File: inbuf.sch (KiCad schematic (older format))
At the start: 21 parts, among them J8 Conn_02x03_Odd_Even, U6 NE5532, U7 NE5532

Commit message: Board is placed and about half-routed
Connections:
- net OUT1: now also U7.1, U7.2 (-); no longer U6.6 (-), U6.7
- net OUT2: now also U7.6 (-), U7.7; no longer U7.1, U7.2 (-)
- net at C34.1, R33.1, R35.1: now also U6.5 (+); no longer U7.5 (+)
- net at R34.2, R36.2: now also U6.6 (-); no longer U7.6 (-)
- net at R32.1, R34.1: now also U6.7; no longer U7.7
- net at J8.4 (Pin_4), R30.1: now also U7.3 (+); no longer U6.5 (+)
- net at J8.3 (Pin_3), R31.1: now also U7.5 (+); no longer U7.3 (+)
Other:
- moved on the sheet: U6B, U7A, U7B
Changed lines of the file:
@@
 L Amplifier_Operational:NE5532 U7
 U 2 1 6159C1D0
-P 3700 4400
-F 0 "U7" H 3700 4800 50  0000 C CNN
-F 1 "NE5532" H 3750 4700 50  0000 C CNN
-F 2 "Housings_DIP:DIP-8_W7.62mm_Socket" H 3700 4400 50  0001 C CNN
-F 3 "http://www.ti.com/lit/ds/symlink/ne5532.pdf" H 3700 4400 50  0001 C CNN
-	2    3700 4400
+P 5950 4400
+F 0 "U7" H 5950 4800 50  0000 C CNN
+F 1 "NE5532" H 6000 4700 50  0000 C CNN
+F 2 "Housings_DIP:DIP-8_W7.62mm_Socket" H 5950 4400 50  0001 C CNN
+F 3 "http://www.ti.com/lit/ds/symlink/ne5532.pdf" H 5950 4400 50  0001 C CNN
+	2    5950 4400
 	1    0    0    -1
 $EndComp
@@
 L Amplifier_Operational:NE5532 U7
 U 1 1 6190D92F
-P 5950 4400
-F 0 "U7" H 5900 4800 50  0000 C CNN
-F 1 "NE5532" H 5950 4700 50  0000 C CNN
-F 2 "Housings_DIP:DIP-8_W7.62mm_Socket" H 5950 4400 50  0001 C CNN
-F 3 "http://www.ti.com/lit/ds/symlink/ne5532.pdf" H 5950 4400 50  0001 C CNN
-	1    5950 4400
+P 5950 1800
+F 0 "U7" H 5900 2200 50  0000 C CNN
+F 1 "NE5532" H 5950 2100 50  0000 C CNN
+F 2 "Housings_DIP:DIP-8_W7.62mm_Socket" H 5950 1800 50  0001 C CNN
+F 3 "http://www.ti.com/lit/ds/symlink/ne5532.pdf" H 5950 1800 50  0001 C CNN
+	1    5950 1800
 	1    0    0    -1
 $EndComp
@@
 L Amplifier_Operational:NE5532 U6
 U 2 1 6190D927
-P 5950 1800
-F 0 "U6" H 5950 2200 50  0000 C CNN
-F 1 "NE5532" H 6000 2100 50  0000 C CNN
-F 2 "Housings_DIP:DIP-8_W7.62mm_Socket" H 5950 1800 50  0001 C CNN
-F 3 "http://www.ti.com/lit/ds/symlink/ne5532.pdf" H 5950 1800 50  0001 C CNN
-	2    5950 1800
-	1    0    0    -1
-$EndComp
+P 3700 4400
+F 0 "U6" H 3700 4800 50  0000 C CNN
+F 1 "NE5532" H 3750 4700 50  0000 C CNN
+F 2 "Housings_DIP:DIP-8_W7.62mm_Socket" H 3700 4400 50  0001 C CNN
+F 3 "http://www.ti.com/lit/ds/symlink/ne5532.pdf" H 3700 4400 50  0001 C CNN
+	2    3700 4400
+	1    0    0    -1
+$EndComp

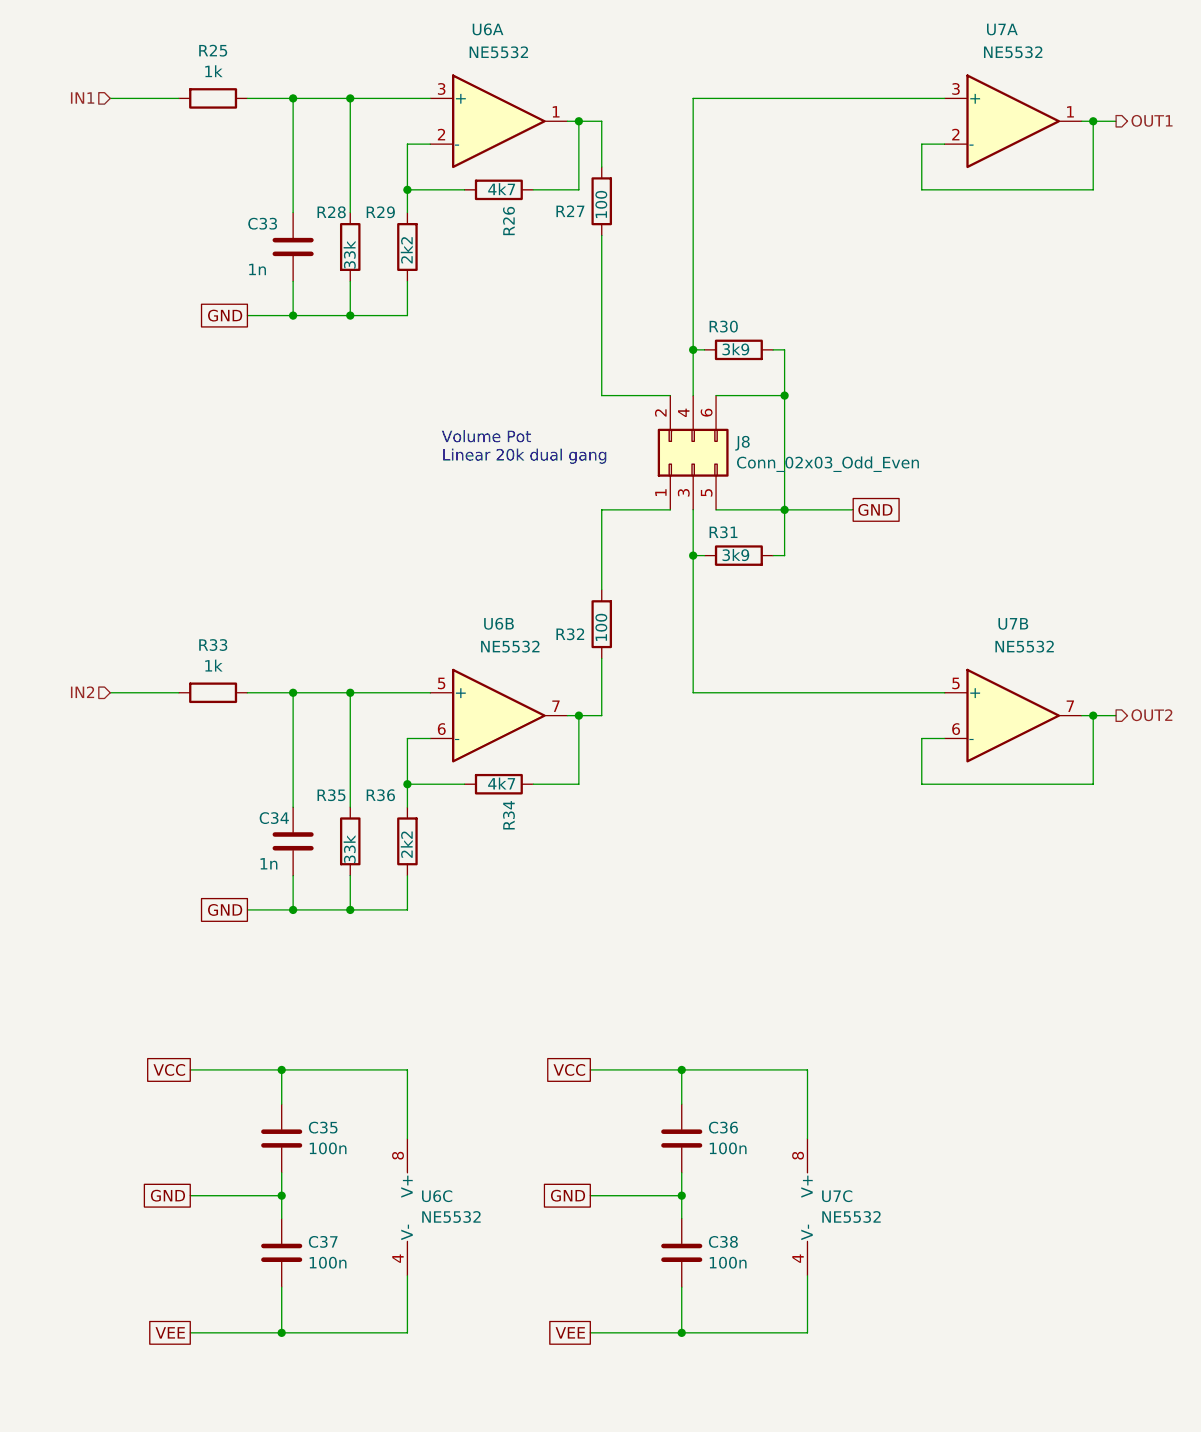
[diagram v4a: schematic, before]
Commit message: Rev.B adds "hum break resistor" in input network
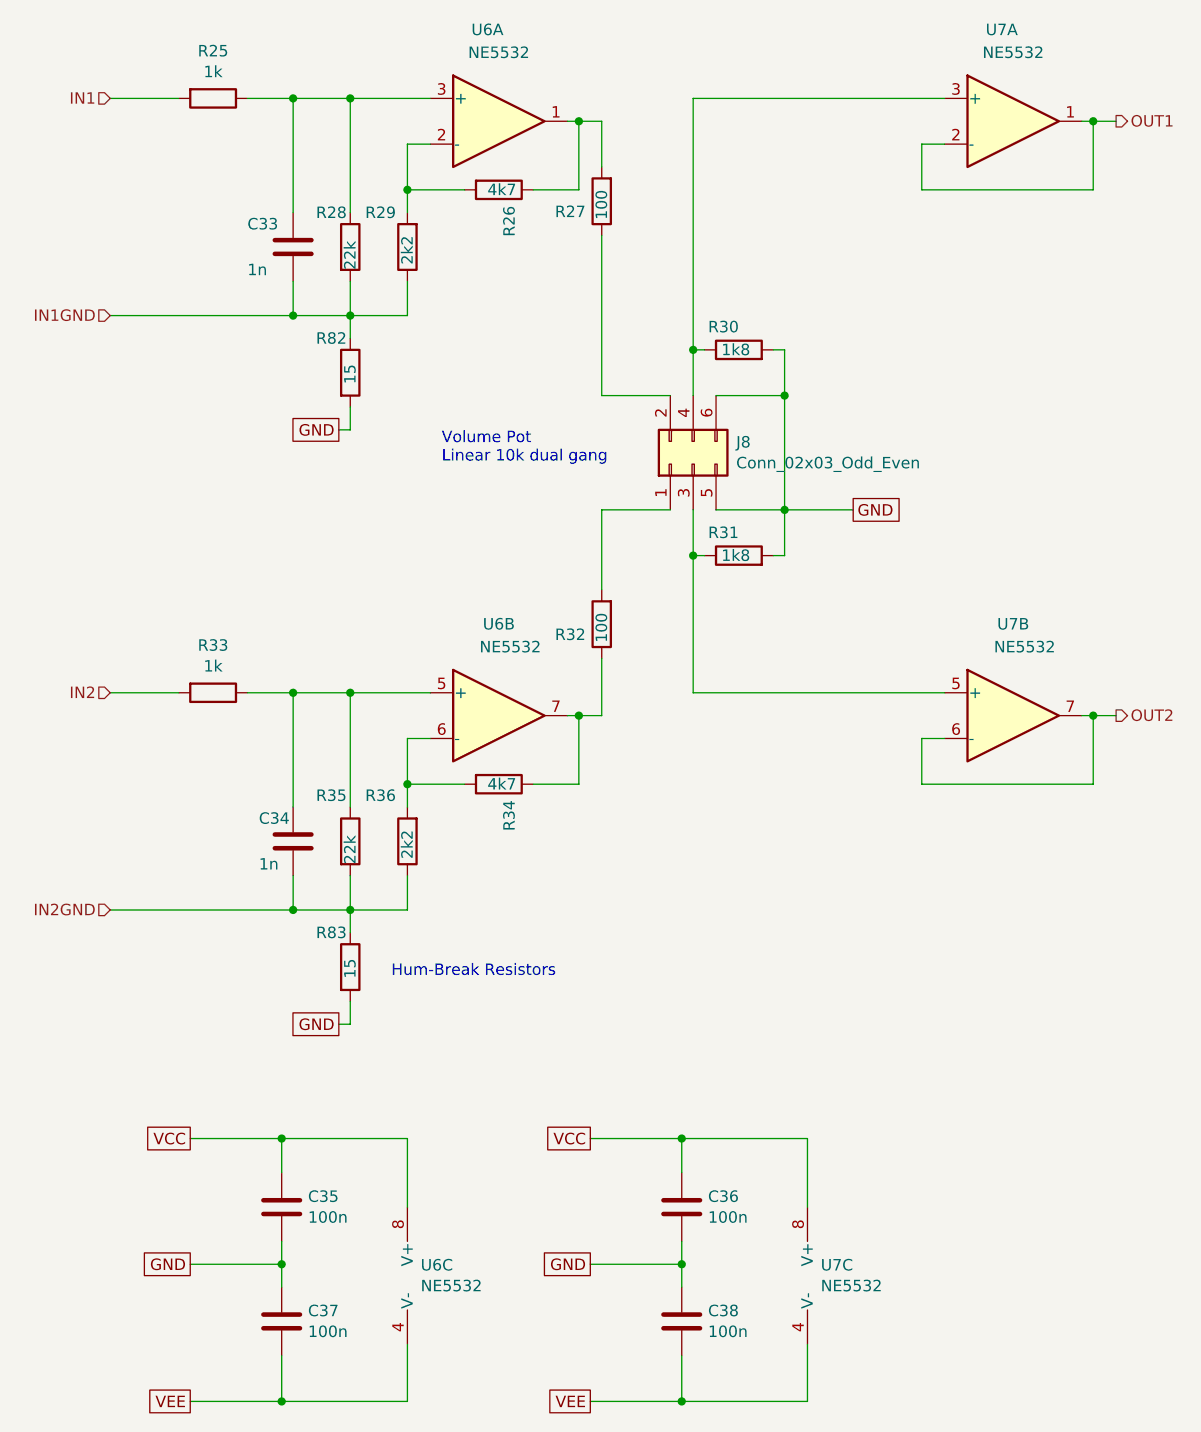
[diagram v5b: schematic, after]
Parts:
- added R82, R83: 15, Resistors_SMD:R_0805, symbol Device:R
- R28, R35: value 33k -> 22k
- R30, R31: value 3k9 -> 1k8
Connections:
- net GND: now also R82.2, R83.2; no longer C33.2, C34.2, R28.2, R29.1, R35.2, R36.1
- new net IN1GND: C33.2, R28.2, R29.1, R82.1
- new net IN2GND: C34.2, R35.2, R36.1, R83.1
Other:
- note added: "Hum-Break Resistors"
- note added: "Volume Pot\nLinear 10k dual gang"
- note removed: "Volume Pot\nLinear 20k dual gang"
- moved on the sheet: C35, C36, C37, C38, U6C, U7C
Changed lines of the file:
@@
 Sheet 6 17
 Title "Input Buffers, 10dB Gain"
-Date "2021-10-03"
-Rev "A"
+Date "2022-01-12"
+Rev "B"
 Comp "Tyrrell Zaibatsu"
 Comment1 ""
@@
 L Amplifier_Operational:NE5532 U6
 U 3 1 6159D2F7
-P 3400 6550
-F 0 "U6" H 3358 6596 50  0000 L CNN
-F 1 "NE5532" H 3358 6505 50  0000 L CNN
-F 2 "Housings_DIP:DIP-8_W7.62mm_Socket" H 3400 6550 50  0001 C CNN
-F 3 "http://www.ti.com/lit/ds/symlink/ne5532.pdf" H 3400 6550 50  0001 C CNN
-	3    3400 6550
+P 3400 6850
+F 0 "U6" H 3358 6896 50  0000 L CNN
+F 1 "NE5532" H 3358 6805 50  0000 L CNN
+F 2 "Housings_DIP:DIP-8_W7.62mm_Socket" H 3400 6850 50  0001 C CNN
+F 3 "http://www.ti.com/lit/ds/symlink/ne5532.pdf" H 3400 6850 50  0001 C CNN
+	3    3400 6850
 	1    0    0    -1
 $EndComp
@@
 P 3050 2350
 F 0 "R28" H 2900 2500 50  0000 L CNN
-F 1 "33k" V 3050 2250 50  0000 L CNN
+F 1 "22k" V 3050 2250 50  0000 L CNN
 F 2 "Resistors_SMD:R_0805" V 2980 2350 50  0001 C CNN
 F 3 "~" H 3050 2350 50  0001 C CNN
@@
 L Device:C C?
 U 1 1 615A8570
-P 2750 6750
+P 2750 7050
 AR Path="/6157B871/615A8570" Ref="C?"  Part="1"
 AR Path="/615961F1/615A8570" Ref="C?"  Part="1"
@@
 AR Path="/61597701/615A8570" Ref="C?"  Part="1"
 AR Path="/6159A74A/615A8570" Ref="C37"  Part="1"
-F 0 "C37" H 2865 6796 50  0000 L CNN
-F 1 "100n" H 2865 6705 50  0000 L CNN
-F 2 "Capacitors_SMD:C_0805" H 2788 6600 50  0001 C CNN
-F 3 "~" H 2750 6750 50  0001 C CNN
-	1    2750 6750
+F 0 "C37" H 2865 7096 50  0000 L CNN
+F 1 "100n" H 2865 7005 50  0000 L CNN
+F 2 "Capacitors_SMD:C_0805" H 2788 6900 50  0001 C CNN
+F 3 "~" H 2750 7050 50  0001 C CNN
+	1    2750 7050
 	1    0    0    -1
 $EndComp
@@
 L Device:C C?
 U 1 1 615A8576
-P 2750 6250
+P 2750 6550
 AR Path="/6157B871/615A8576" Ref="C?"  Part="1"
 AR Path="/615961F1/615A8576" Ref="C?"  Part="1"
@@
 AR Path="/61597701/615A8576" Ref="C?"  Part="1"
 AR Path="/6159A74A/615A8576" Ref="C35"  Part="1"
-F 0 "C35" H 2865 6296 50  0000 L CNN
-F 1 "100n" H 2865 6205 50  0000 L CNN
-F 2 "Capacitors_SMD:C_0805" H 2788 6100 50  0001 C CNN
-F 3 "~" H 2750 6250 50  0001 C CNN
-	1    2750 6250
-	1    0    0    -1
-$EndComp
-Wire Wire Line
-	2750 6400 2750 6500
-Wire Wire Line
-	2350 6500 2750 6500
-Connection ~ 2750 6500
-Wire Wire Line
-	2750 6500 2750 6600
-Text GLabel 2350 6500 0    50   UnSpc ~ 0
+F 0 "C35" H 2865 6596 50  0000 L CNN
+F 1 "100n" H 2865 6505 50  0000 L CNN
+F 2 "Capacitors_SMD:C_0805" H 2788 6400 50  0001 C CNN
+F 3 "~" H 2750 6550 50  0001 C CNN
+	1    2750 6550
+	1    0    0    -1
+$EndComp
+Wire Wire Line
+	2750 6700 2750 6800
+Wire Wire Line
+	2350 6800 2750 6800
+Connection ~ 2750 6800
+Wire Wire Line
+	2750 6800 2750 6900
+Text GLabel 2350 6800 0    50   UnSpc ~ 0
 GND
-Text GLabel 2350 5950 0    50   UnSpc ~ 0
+Text GLabel 2350 6250 0    50   UnSpc ~ 0
 VCC
-Text GLabel 2350 7100 0    50   UnSpc ~ 0
+Text GLabel 2350 7400 0    50   UnSpc ~ 0
 VEE
 Wire Wire Line
-	2350 5950 2750 5950
-Wire Wire Line
-	2750 5950 2750 6100
-Wire Wire Line
-	2350 7100 2750 7100
-Wire Wire Line
-	2750 7100 2750 6900
-Wire Wire Line
-	2750 5950 3300 5950
-Connection ~ 2750 5950
-Wire Wire Line
-	2750 7100 3300 7100
-Connection ~ 2750 7100
-Wire Wire Line
-	3300 5950 3300 6250
-Wire Wire Line
-	3300 6850 3300 7100
-Text GLabel 2600 2650 0    50   UnSpc ~ 0
+	2350 6250 2750 6250
+Wire Wire Line
+	2750 6250 2750 6400
+Wire Wire Line
+	2350 7400 2750 7400
+Wire Wire Line
+	2750 7400 2750 7200
+Wire Wire Line
+	2750 6250 3300 6250
+Connection ~ 2750 6250
+Wire Wire Line
+	2750 7400 3300 7400
+Connection ~ 2750 7400
+Wire Wire Line
+	3300 6250 3300 6550
+Wire Wire Line
+	3300 7150 3300 7400
+Text GLabel 3000 3150 0    50   UnSpc ~ 0
 GND
-Wire Wire Line
-	2800 2650 2600 2650
 Connection ~ 2800 2650
 Text HLabel 2000 1700 0    50   Input ~ 0
@@
 	2000 4300 2300 4300
 Connection ~ 2800 5250
-Wire Wire Line
-	2800 5250 2600 5250
-Text GLabel 2600 5250 0    50   UnSpc ~ 0
-GND
 Wire Wire Line
 	2800 5250 2800 5100
@@
 P 3050 4950
 F 0 "R35" H 2900 5150 50  0000 L CNN
-F 1 "33k" V 3050 4850 50  0000 L CNN
+F 1 "22k" V 3050 4850 50  0000 L CNN
 F 2 "Resistors_SMD:R_0805" V 2980 4950 50  0001 C CNN
 F 3 "~" H 3050 4950 50  0001 C CNN
@@
 $EndComp
 Text Notes 3450 3300 0    50   ~ 0
-Volume Pot\nLinear 20k dual gang
+Volume Pot\nLinear 10k dual gang
 Wire Wire Line
 	4150 3500 4450 3500
@@
 Wire Wire Line
 	5550 4700 6300 4700
-$Comp
-L Device:R R31
-U 1 1 6192D4B9
-P 4750 3700
-F 0 "R31" V 4850 3700 50  0000 L CNN
-F 1 "3k9" V 4750 3650 50  0000 L CNN
-F 2 "Resistors_SMD:R_0805" V 4680 3700 50  0001 C CNN
-F 3 "~" H 4750 3700 50  0001 C CNN
-	1    4750 3700
-	0    -1   -1   0
-$EndComp
 $Comp
 L Device:R R30
@@
 P 4750 2800
 F 0 "R30" V 4850 2800 50  0000 L CNN
-F 1 "3k9" V 4750 2750 50  0000 L CNN
+F 1 "1k8" V 4750 2750 50  0000 L CNN
 F 2 "Resistors_SMD:R_0805" V 4680 2800 50  0001 C CNN
 F 3 "~" H 4750 2800 50  0001 C CNN
@@
 L Amplifier_Operational:NE5532 U7
 U 3 1 61982144
-P 5150 6550
-F 0 "U7" H 5108 6596 50  0000 L CNN
-F 1 "NE5532" H 5108 6505 50  0000 L CNN
-F 2 "Housings_DIP:DIP-8_W7.62mm_Socket" H 5150 6550 50  0001 C CNN
-F 3 "http://www.ti.com/lit/ds/symlink/ne5532.pdf" H 5150 6550 50  0001 C CNN
-	3    5150 6550
+P 5150 6850
+F 0 "U7" H 5108 6896 50  0000 L CNN
+F 1 "NE5532" H 5108 6805 50  0000 L CNN
+F 2 "Housings_DIP:DIP-8_W7.62mm_Socket" H 5150 6850 50  0001 C CNN
+F 3 "http://www.ti.com/lit/ds/symlink/ne5532.pdf" H 5150 6850 50  0001 C CNN
+	3    5150 6850
 	1    0    0    -1
 $EndComp
@@
 L Device:C C?
 U 1 1 6198214A
-P 4500 6750
+P 4500 7050
 AR Path="/6157B871/6198214A" Ref="C?"  Part="1"
 AR Path="/615961F1/6198214A" Ref="C?"  Part="1"
@@
 AR Path="/61597701/6198214A" Ref="C?"  Part="1"
 AR Path="/6159A74A/6198214A" Ref="C38"  Part="1"
-F 0 "C38" H 4615 6796 50  0000 L CNN
-F 1 "100n" H 4615 6705 50  0000 L CNN
-F 2 "Capacitors_SMD:C_0805" H 4538 6600 50  0001 C CNN
-F 3 "~" H 4500 6750 50  0001 C CNN
-	1    4500 6750
+F 0 "C38" H 4615 7096 50  0000 L CNN
+F 1 "100n" H 4615 7005 50  0000 L CNN
+F 2 "Capacitors_SMD:C_0805" H 4538 6900 50  0001 C CNN
+F 3 "~" H 4500 7050 50  0001 C CNN
+	1    4500 7050
 	1    0    0    -1
 $EndComp
@@
 L Device:C C?
 U 1 1 61982150
-P 4500 6250
+P 4500 6550
 AR Path="/6157B871/61982150" Ref="C?"  Part="1"
 AR Path="/615961F1/61982150" Ref="C?"  Part="1"
@@
 AR Path="/61597701/61982150" Ref="C?"  Part="1"
 AR Path="/6159A74A/61982150" Ref="C36"  Part="1"
-F 0 "C36" H 4615 6296 50  0000 L CNN
-F 1 "100n" H 4615 6205 50  0000 L CNN
-F 2 "Capacitors_SMD:C_0805" H 4538 6100 50  0001 C CNN
-F 3 "~" H 4500 6250 50  0001 C CNN
-	1    4500 6250
-	1    0    0    -1
-$EndComp
-Wire Wire Line
-	4500 6400 4500 6500
-Wire Wire Line
-	4100 6500 4500 6500
-Connection ~ 4500 6500
-Wire Wire Line
-	4500 6500 4500 6600
-Text GLabel 4100 6500 0    50   UnSpc ~ 0
+F 0 "C36" H 4615 6596 50  0000 L CNN
+F 1 "100n" H 4615 6505 50  0000 L CNN
+F 2 "Capacitors_SMD:C_0805" H 4538 6400 50  0001 C CNN
+F 3 "~" H 4500 6550 50  0001 C CNN
+	1    4500 6550
+	1    0    0    -1
+$EndComp
+Wire Wire Line
+	4500 6700 4500 6800
+Wire Wire Line
+	4100 6800 4500 6800
+Connection ~ 4500 6800
+Wire Wire Line
+	4500 6800 4500 6900
+Text GLabel 4100 6800 0    50   UnSpc ~ 0
 GND
-Text GLabel 4100 5950 0    50   UnSpc ~ 0
+Text GLabel 4100 6250 0    50   UnSpc ~ 0
 VCC
-Text GLabel 4100 7100 0    50   UnSpc ~ 0
+Text GLabel 4100 7400 0    50   UnSpc ~ 0
 VEE
 Wire Wire Line
-	4100 5950 4500 5950
-Wire Wire Line
-	4500 5950 4500 6100
-Wire Wire Line
-	4100 7100 4500 7100
-Wire Wire Line
-	4500 7100 4500 6900
-Wire Wire Line
-	4500 5950 5050 5950
-Connection ~ 4500 5950
-Wire Wire Line
-	4500 7100 5050 7100
-Connection ~ 4500 7100
-Wire Wire Line
-	5050 5950 5050 6250
-Wire Wire Line
-	5050 6850 5050 7100
+	4100 6250 4500 6250
+Wire Wire Line
+	4500 6250 4500 6400
+Wire Wire Line
+	4100 7400 4500 7400
+Wire Wire Line
+	4500 7400 4500 7200
+Wire Wire Line
+	4500 6250 5050 6250
+Connection ~ 4500 6250
+Wire Wire Line
+	4500 7400 5050 7400
+Connection ~ 4500 7400
+Wire Wire Line
+	5050 6250 5050 6550
+Wire Wire Line
+	5050 7150 5050 7400
 Text GLabel 5250 3500 2    50   UnSpc ~ 0
 GND
@@
 Wire Wire Line
 	4550 1700 4550 2800
+Text HLabel 2000 2650 0    50   Input ~ 0
+IN1GND
+Text HLabel 2000 5250 0    50   Input ~ 0
+IN2GND
+Wire Wire Line
+	2000 2650 2800 2650
+$Comp
+L Device:R R82
+U 1 1 6207CE49
+P 3050 2900
+F 0 "R82" H 2900 3050 50  0000 L CNN
+F 1 "15" V 3050 2850 50  0000 L CNN
+F 2 "Resistors_SMD:R_0805" V 2980 2900 50  0001 C CNN
+F 3 "~" H 3050 2900 50  0001 C CNN
+	1    3050 2900
+	1    0    0    -1
+$EndComp
+Wire Wire Line
+	3050 2650 3050 2750
+Wire Wire Line
+	3050 3050 3050 3150
+Wire Wire Line
+	3050 3150 3000 3150
+Text GLabel 3000 5750 0    50   UnSpc ~ 0
+GND
+$Comp
+L Device:R R83
+U 1 1 62088AFF
+P 3050 5500
+F 0 "R83" H 2900 5650 50  0000 L CNN
+F 1 "15" V 3050 5450 50  0000 L CNN
+F 2 "Resistors_SMD:R_0805" V 2980 5500 50  0001 C CNN
+F 3 "~" H 3050 5500 50  0001 C CNN
+	1    3050 5500
+	1    0    0    -1
+$EndComp
+Wire Wire Line
+	3050 5250 3050 5350
+Wire Wire Line
+	3050 5650 3050 5750
+Wire Wire Line
+	3050 5750 3000 5750
+Wire Wire Line
+	2000 5250 2800 5250
+Text Notes 3950 5550 2    50   ~ 0
+Hum-Break Resistors
+$Comp
+L Device:R R31
+U 1 1 6192D4B9
+P 4750 3700
+F 0 "R31" V 4850 3700 50  0000 L CNN
+F 1 "1k8" V 4750 3650 50  0000 L CNN
+F 2 "Resistors_SMD:R_0805" V 4680 3700 50  0001 C CNN
+F 3 "~" H 4750 3700 50  0001 C CNN
+	1    4750 3700
+	0    -1   -1   0
+$EndComp
 $EndSCHEMATC
